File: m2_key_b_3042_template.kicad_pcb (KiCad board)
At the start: 2 copper layers, 42 x 30 mm, 2 parts, among them J1 M.2_Key_B

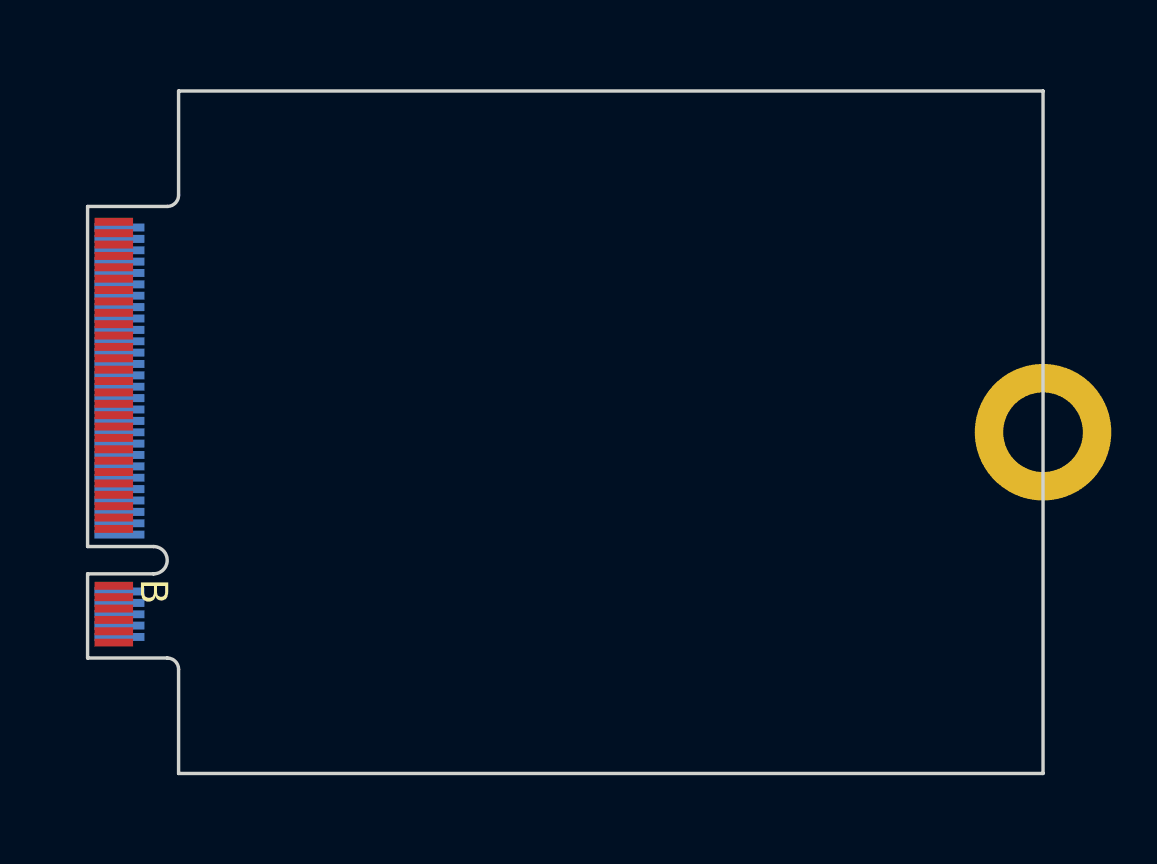
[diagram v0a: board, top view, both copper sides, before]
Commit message: Include MHF4 coax connectors for the baseband, diversity, and GNSS antennae
Improved the soldermask and mounting hole.
Included silkscreen designating the component area.
Antennae MHF4 coax connectors show what orientation they need to be placed in (chamfer).
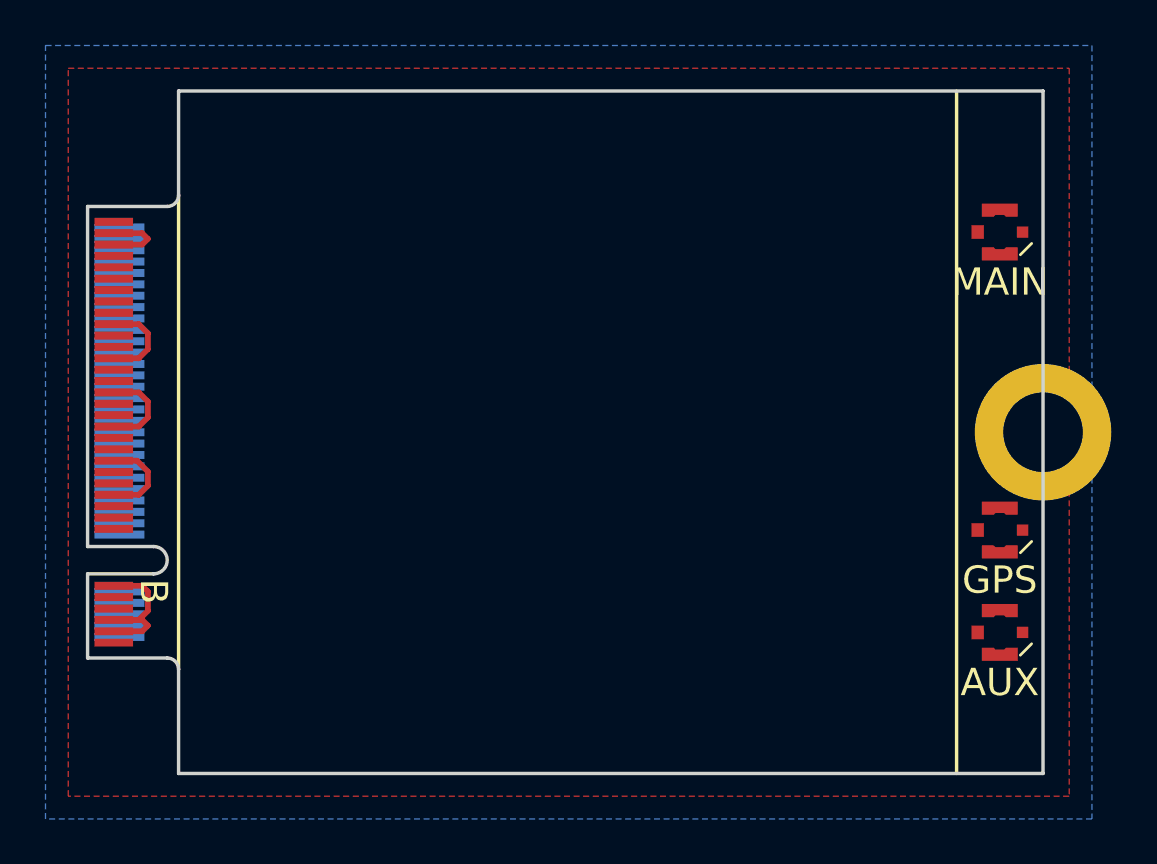
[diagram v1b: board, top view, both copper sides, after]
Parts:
- added ANT1: Conn_Coaxial, m2_key_b_3042:MHF4_20449-001E, F.Cu at (158.9, 103.8)
- added ANT2: Conn_Coaxial, m2_key_b_3042:MHF4_20449-001E, F.Cu at (158.9, 99.3)
- added ANT4: Conn_Coaxial, m2_key_b_3042:MHF4_20449-001E, F.Cu at (158.9, 86.2)
- J1: footprint m2_key_b_3042:m2_key_b_3042_gold_fingers -> m2_key_b_3042:M.2_Key_B_Gold_Fingers
- REF**: footprint Mounting_Holes:MountingHole_3.5mm_Pad -> m2_key_b_3042:M.2_Mounting_Hole
- moved REF** 0.15 mm to (160.8, 95.0), turned to 90 degrees
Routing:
- net GND: track 0.00 -> 25.4 mm
- added copper zone on B.Cu, net GND
- added copper zone on F.Cu, net GND
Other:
- net class Default: clearance 0.2 -> 0.15
- rule trace_clearance: 0.2 -> 0.15
- board text added: "3042 typically 8 layers with 1oz copper"
- board text added: "AUX"
- board text added: "GPS"
- board text added: "MAIN"
